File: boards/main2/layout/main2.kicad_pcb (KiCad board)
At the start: 4 copper layers, 50 x 100 mm, 212 parts, among them IC1 STM32H725RGV6, IC2 LSM6DSVTR, IC6 STSPIN958TR, IC7 L6981C33DR, IC8 DRV8874PWPR, IC9 DRV8874PWPR, J1 B02B-PASK(LF)(SN), M1 B02B-PASK(LF)(SN), M2 B02B-PASK(LF)(SN), M3 B02B-PASK(LF)(SN), Q1 AO3400A, Q2 AO3400A, Q3 AO3400A, Q4 AO3400A, Q5 AO3400A, Q6 HSBB3072, Q8 AO3401A, Q9 AO3400A, SW1 DSHP04TJGER, SW2 GT-TC048B-H025-L1, SW3 GT-TC048B-H025-L1, SW4 SK-12D29-G060, U10 INA241A2IDGKR, U11 INA241A2IDGKR, U12 TLV9001IDBVR, U13 ESP32-S3-MINI-1-N8, U2 GT-USB-7010ASV, U6 USBLC6-2SC6, U8 ADP7142ACPZN3.3-R7

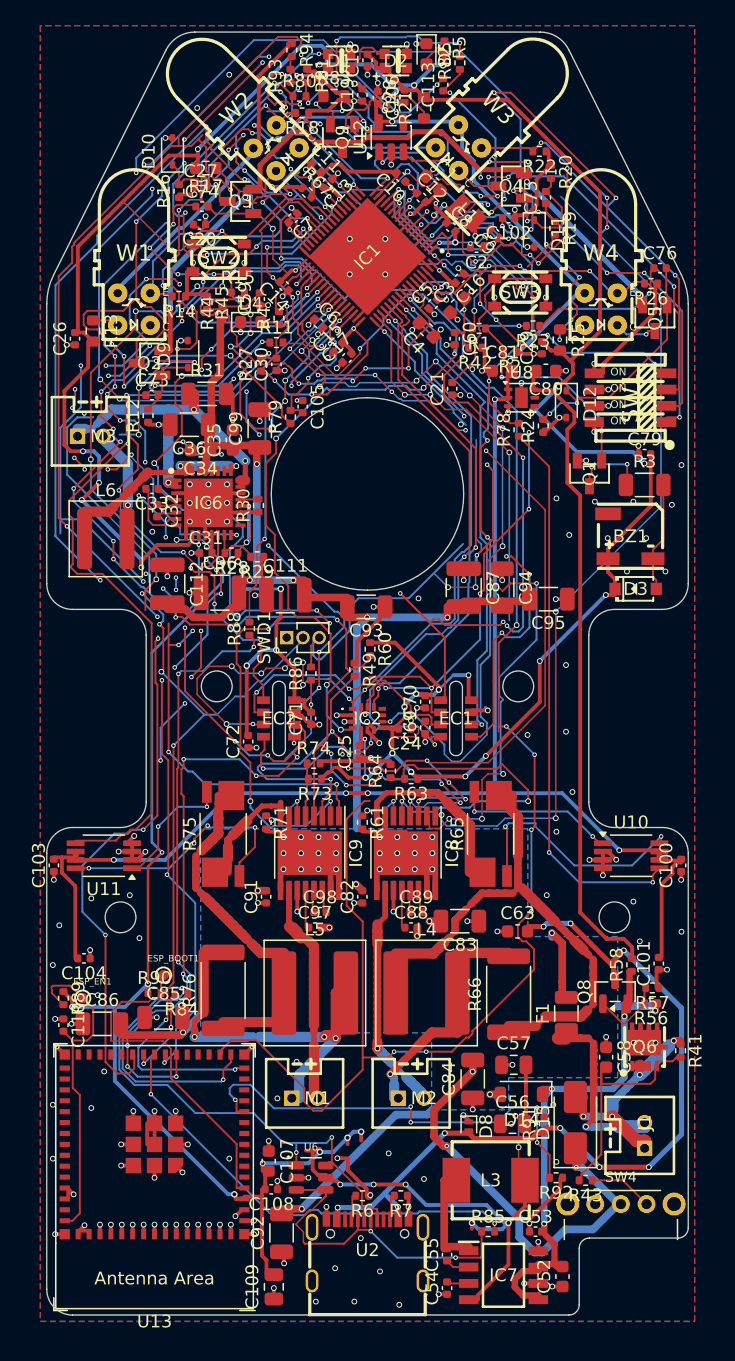
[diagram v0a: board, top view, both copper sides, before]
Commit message: 🐛 Fix main2's review findings and settle its open doubts
Schematic and parts:
- Battery input: F1 is a 12 A Littelfuse 501 (0501012.WR1). C58 now sits
  gate-source with C114 gate-drain, so Q6 stays off at plug-in. D16 clamps
  Q8's VGS. R44/R45 are 10k/2k, so VBAT can't float up on USB alone.
- Capacitors: VBAT and VSYS use 1210/0805 50 V parts, sized with Samsung's
  DC-bias curves. C109 is fitted.
- Drivers: R66/R76 are removed (the chokes are needed). ITRIP and the fan
  limit are retuned. The INA241 R_iso is 150 Ohm.
- Rails are declared as ranges, and the abs-max checks run under the TVS
  clamp.
- STM32 pin swaps for routing: the wall selectors move to TIM3,
  Motor_Left_EN to TIM8_CH2 and LED_ARGB to TIM17. CubeMX 6.18.1 confirms
  the map.
- firmware_changes.toml registers the matching firmware changes: the ADC
  0.7 us sampling time, the TIM4-triggered DAC, the fan's 50 kHz start, a
  wheel-sign self-check, VDDA tracking, contest mode, the debug halt and
  others.

Layout:
- USB D+/D- are routed as a coupled pair. The track floor is 0.12 mm.
- Stubs and detours are trimmed. The In2 VCORE/3V3_D islands are shrunk.
- The board is notched under the ESP32 antenna.
- Ground stitching, thermal reliefs, open thermal vias with split paste,
  DRV8874 heat islands and teardrops are added.
- 11 joins remain for hand-routing (layout README, Open items).

Doubts are closed by datasheets, vendor SPICE models and new research
calculations instead of bench TODOs. Tests cover each review item.
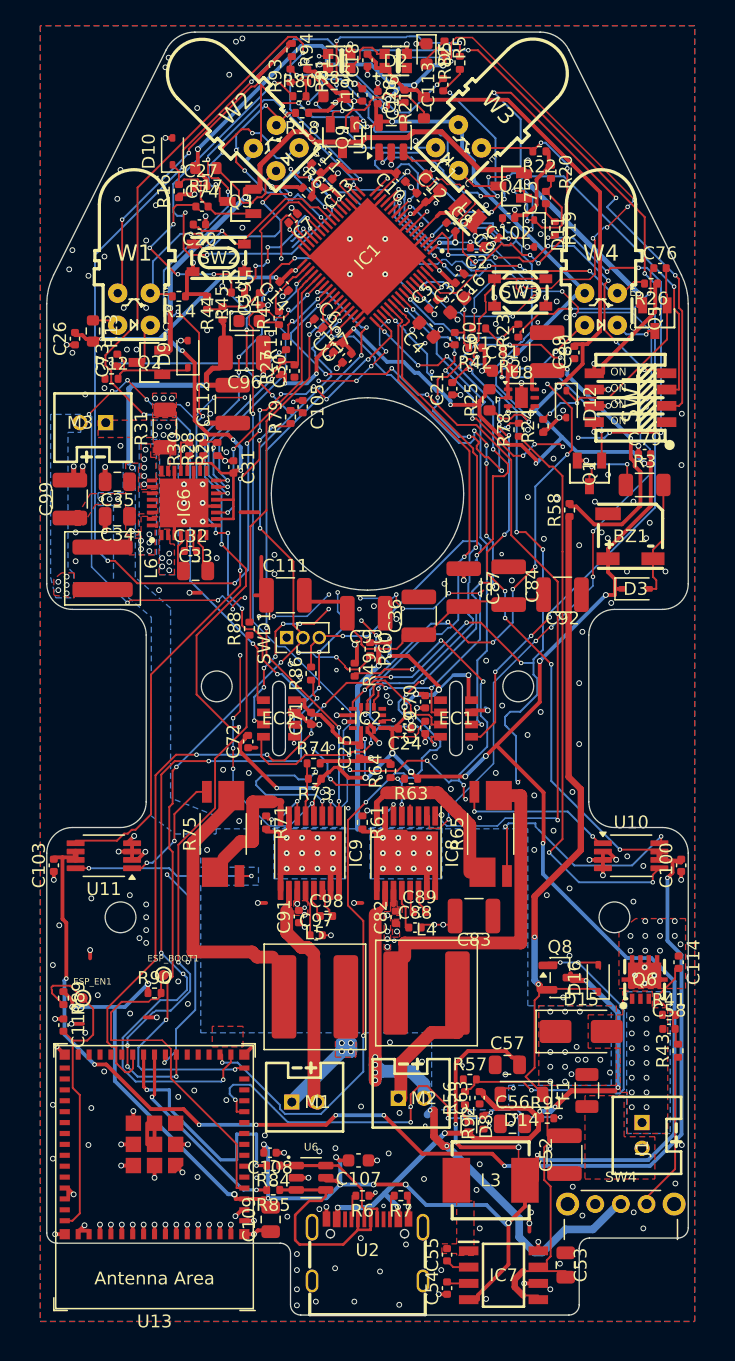
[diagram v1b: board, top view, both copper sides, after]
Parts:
- removed C101, C104: 10nF 10% 50V X7R, stdlib_kicad-footprints_Capacitor_SMD:C_0402_1005Metric
- removed C85, C86, C94, C95: 10uF 10% 50V X7R, stdlib_kicad-footprints_Capacitor_SMD:C_1206_3216Metric
- removed R66, R76: 0 1W, stdlib_kicad-footprints_Resistor_SMD:R_2512_6332Metric
- added C114: 1nF 5% 50V C0G, stdlib_kicad-footprints_Capacitor_SMD:C_0402_1005Metric, F.Cu at (172.8, 132.5)
- added D16: 10V zener, Team-Micras_MicrasPCB_components_diodes_BZT52C10S:D_SOD-323, F.Cu at (166.5, 133.8)
- C33, C53: value 1uF 10% 25V X5R -> 1uF 10% 50V X7R; footprint stdlib_kicad-footprints_Capacitor_SMD:C_0402_1005Metric -> stdlib_kicad-footprints_Capacitor_SMD:C_0805_2012Metric
- C34, C35: footprint stdlib_kicad-footprints_Capacitor_SMD:C_0603_1608Metric -> stdlib_kicad-footprints_Capacitor_SMD:C_0805_2012Metric
- C36, C83, C84, C92, C93, C99: footprint stdlib_kicad-footprints_Capacitor_SMD:C_1206_3216Metric -> stdlib_kicad-footprints_Capacitor_SMD:C_1210_3225Metric
- C52, C80: value 10uF 20% 25V X5R -> 10uF 10% 50V X7R; footprint stdlib_kicad-footprints_Capacitor_SMD:C_0603_1608Metric -> stdlib_kicad-footprints_Capacitor_SMD:C_1210_3225Metric
- C58: value 47nF 10% 50V X7R -> 100nF 10% 50V X7R; footprint stdlib_kicad-footprints_Capacitor_SMD:C_0603_1608Metric -> stdlib_kicad-footprints_Capacitor_SMD:C_0402_1005Metric
- C63: value 10uF 20% 25V X5R -> 1uF 10% 25V X5R; footprint stdlib_kicad-footprints_Capacitor_SMD:C_0603_1608Metric -> stdlib_kicad-footprints_Capacitor_SMD:C_0402_1005Metric
- D3: value 1N4148W -> 1N4148WS; footprint Team-Micras_MicrasPCB_components_hongjiacheng_1N4148W:SOD-123_L2.7-W1.6-LS3.7-FD -> Team-Micras_MicrasPCB_components_cj_1N4148WS:D_SOD-323
- D8: value 5V TVS Diode -> 6V TVS Diode
- F1: value 20A 32V fast -> 12A 32V fast; footprint Team-Micras_MicrasPCB_components_littelfuse_0501020:Fuse_Littelfuse_501_1206 -> Team-Micras_MicrasPCB_components_littelfuse_05010xx:Fuse_Littelfuse_501_1206
- IC1: footprint Team-Micras_MicrasPCB_components_st_STM32H725RGV6:QFN-68-1EP_8x8mm_P0.4mm_EP6.5x6.5mm -> Team-Micras_MicrasPCB_components_st_STM32H725RGV6:QFN-68-1EP_8x8mm_P0.4mm_EP6.5x6.5mm_SplitPaste
- IC6: footprint Team-Micras_MicrasPCB_components_st_STSPIN958:QFN50P500X500X100-33N-D -> Team-Micras_MicrasPCB_components_st_STSPIN958:QFN50P500X500X100-33N-D_SplitPaste
- Q6: footprint Team-Micras_MicrasPCB_components_huashuo_HSBB3072:PRPAK-8_L3.0-W3.0-P0.65-BL-EP -> Team-Micras_MicrasPCB_components_huashuo_HSBB3072:PRPAK-8_L3.0-W3.0-P0.65-BL-EP_SplitPaste
- R28: value 22k 1% -> 4.7k 1%
- R29: value 9.1k 1% -> 2k 1%
- R44: value 100k 1% -> 10k 1%
- R45: value 20k 1% -> 2k 1%
- R63, R73: value 5.6k 1% -> 4.7k 1%
- R64, R74: value 24k 1% -> 20k 1%
- R78, R79: value 100 1% -> 150 1%
- moved C92 54.4 mm to (163.7, 103.9), turned to 180 degrees
- moved C84 38.6 mm to (159.5, 103.2), turned to -90 degrees
- moved R58 35.8 mm to (164.3, 97.3)
- moved C36 23.3 mm to (152.5, 105.5), turned to 90 degrees
- moved C96 18.8 mm to (138.9, 85.0), turned to 180 degrees
- moved R85 17.1 mm to (141.2, 150.3), turned to 180 degrees
- moved R56 16.3 mm to (156.1, 143.1), turned to 90 degrees
- moved R57 15.9 mm to (156.5, 141.6), turned to 0 degrees
- moved C99 15.8 mm to (125.3, 96.4)
- moved R84 15.1 mm to (141.2, 148.4)
- moved C112 14.9 mm to (138.0, 89.0), turned to 90 degrees
- moved C63 13.3 mm to (157.2, 143.1), turned to 90 degrees
- moved R43 12.4 mm to (172.7, 139.4), turned to 90 degrees
- moved C35 9.57 mm to (129.0, 95.1), turned to 180 degrees
- moved C52 9.50 mm to (163.9, 147.5)
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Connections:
- C58 pad 1: GND -> GND_BAT
- D3 pad 1: PERIPHERALS.BUZZER_COIL -> 3V3_D
- D3 pad 2: 3V3_D -> PERIPHERALS.BUZZER_COIL
- IC1 pad 29: ESP_Flow -> Wall_Sensor_PWM_1
- IC1 pad 32: Encoder_Right_CSn -> IMU_INT1
- IC1 pad 40: LED_ARGB -> Motor_Left_PH
- IC1 pad 42: Motor_Left_PH -> Wall_Sensor_PWM_0
- IC1 pad 44: Motor_Right_PH -> ESP_Flow
- IC1 pad 59: IMU_INT2 -> Wall_Sensor_PWM_2
- IC1 pad 60: IMU_INT1 -> Wall_Sensor_PWM_3
- IC1 pad 61: Wall_Sensor_PWM_0 -> IMU_INT2
- IC1 pad 62: Wall_Sensor_PWM_1 -> Encoder_Right_CSn
- IC1 pad 64: Wall_Sensor_PWM_2 -> Motor_Right_PH
- IC1 pad 65: Wall_Sensor_PWM_3 -> LED_ARGB
- U13 pad 17: Reset -> ESP_Flow
- U13 pad 25: ESP_Flow -> Reset
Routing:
- net Encoder_Right_ABI_B: track 48.8 -> 168.1 mm, vias 6 -> 16
- net Encoder_Left_ABI_A: track 117.2 -> 1.99 mm, vias 13 -> 1
- net Motor_Right_EN: track 156.2 -> 66.7 mm, vias 10 -> 7
- net Encoder_Right_CSn: track 68.7 -> 2.47 mm, vias 6 -> 1
- net VBAT: track 146.4 -> 83.2 mm, vias 20 -> 36
- net Motors_nFault: track 98.8 -> 36.0 mm, vias 20 -> 8
- net UART4_TX: track 75.3 -> 18.7 mm, vias 11 -> 2
- net Motors_Enable: track 97.8 -> 48.0 mm, vias 15 -> 9
- net IMU_INT1: track 52.3 -> 6.57 mm, vias 6 -> 1
- net 3V3_A: track 182.9 -> 224.4 mm, vias 10 -> 23
- net Fan_PWM: track 62.0 -> 22.1 mm, vias 9 -> 2
- net VSYS: track 37.3 -> 72.7 mm, vias 3 -> 2
- net SPI_SCK: track 66.1 -> 100.0 mm, vias 9 -> 25
- net Switch_0: track 36.5 -> 3.09 mm, vias 6 -> 1
- net SWDIO: track 123.2 -> 91.1 mm, vias 20 -> 11
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- added copper zone on F.Cu, net BAT_P
- added copper zone on B.Cu, net DRIVERS.FAN_LSS
- added copper zone on F.Cu, net DRIVERS.FAN_LSS
- added copper zone on B.Cu, net DRIVERS.FAN_MOTOR
- added copper zone on F.Cu, net DRIVERS.FAN_MOTOR
- added copper zone on B.Cu, net DRIVERS.FAN_OUT
- added copper zone on F.Cu, net DRIVERS.FAN_OUT
- added copper zone on F.Cu, net DRIVERS.MOTOR_L_TERMINAL
- added copper zone on B.Cu, net GND_BAT
- added copper zone on F.Cu, net GND_BAT
- added copper zone on F.Cu, net REGULATORS.BUCK_SW
- added copper zone on F.Cu, net VBAT
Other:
- outline, holes or cut-outs redrawn
